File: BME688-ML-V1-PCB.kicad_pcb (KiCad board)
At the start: 2 copper layers, 25.4 x 25.4 mm, 33 parts, among them SW1 434133025816, U1 STM32L431KBU6TR, U2 BME688, U3 BME688

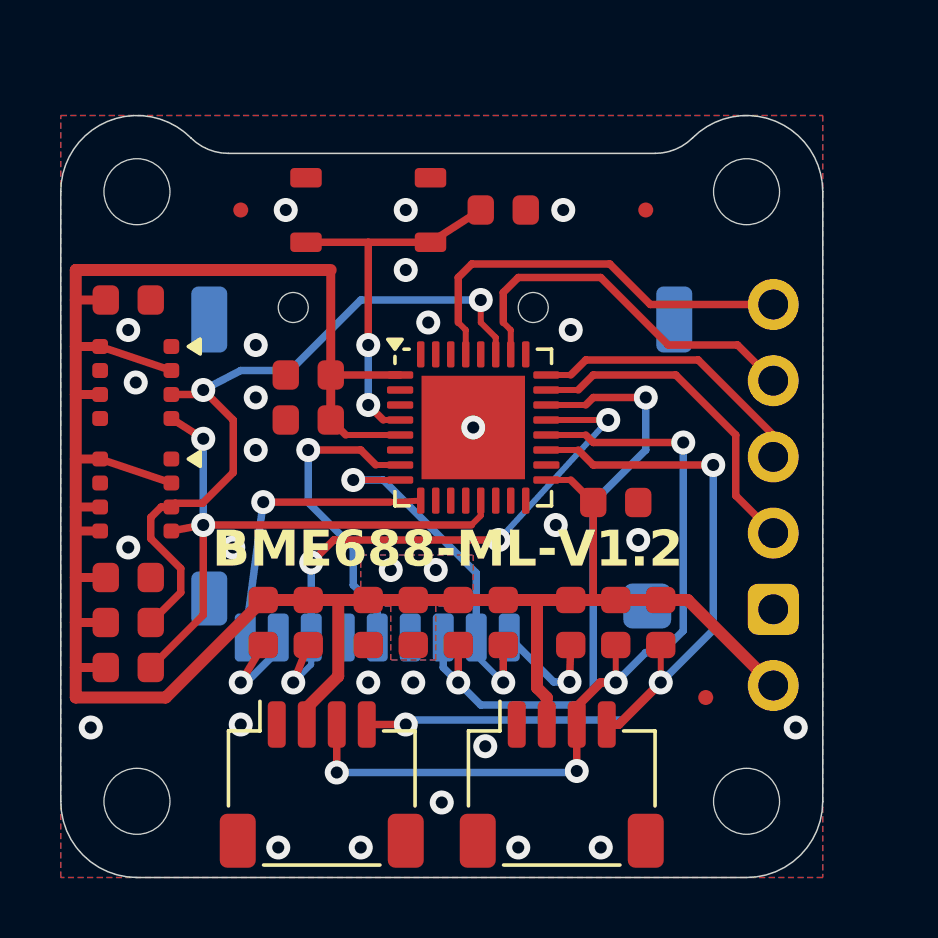
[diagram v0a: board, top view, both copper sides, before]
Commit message: fillet tracks for more beauty
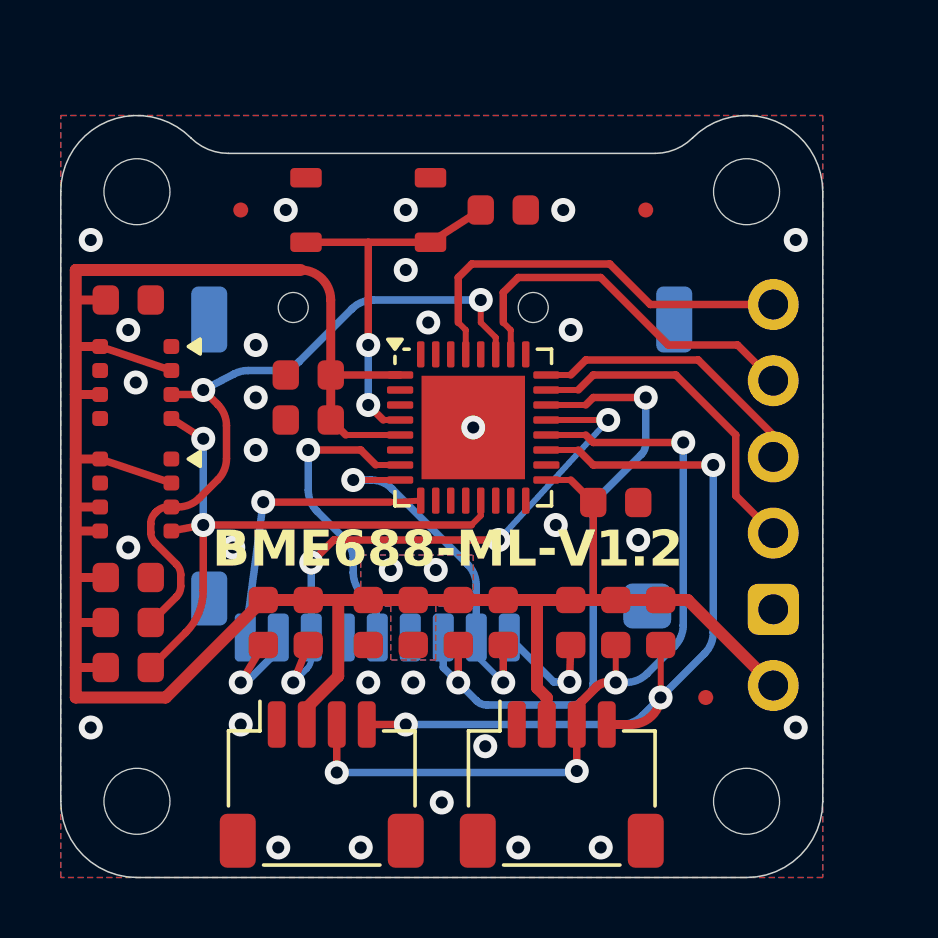
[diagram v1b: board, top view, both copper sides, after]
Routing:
- net I2C3-SDA: track 24.4 -> 23.7 mm
- net I2C1-SCL: track 27.8 -> 28.3 mm
- net GND: vias 27 -> 29

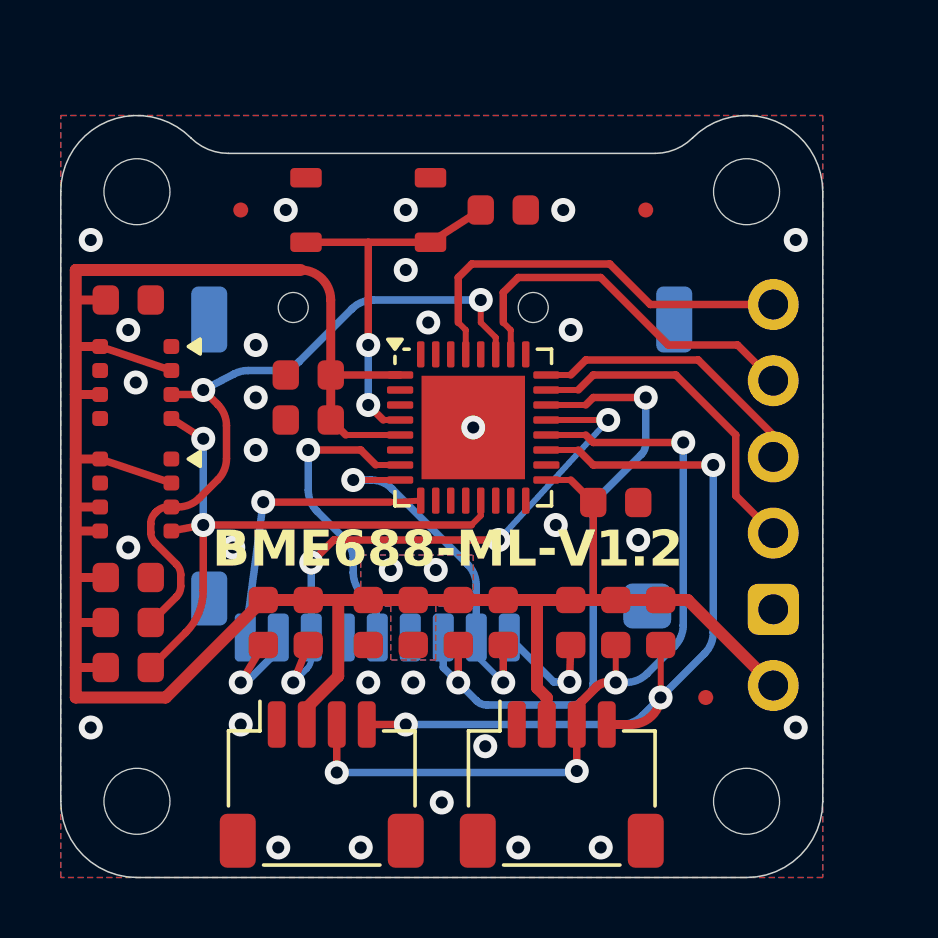
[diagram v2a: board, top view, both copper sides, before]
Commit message: Add #3 and fix #5
Add application button
Add RGB led
Move SD-card connector to align inserted card with PCB edge
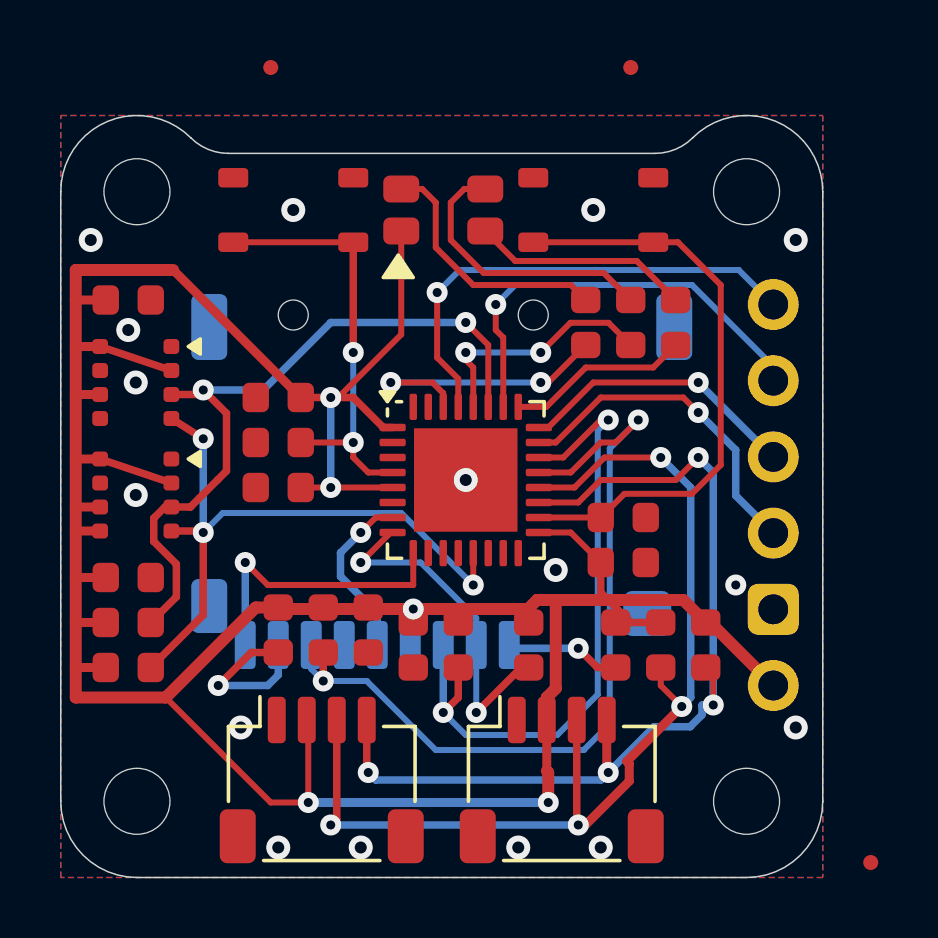
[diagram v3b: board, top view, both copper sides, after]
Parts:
- added C9: KGM15AR71C104KT, 1projectLibrary:C_0603_nominal, F.Cu at (133.1, 76.9)
- added D1: LED_RGBA_150141M173100, 1projectLibrary:RGB_LED_150141M173100, F.Cu at (127.0, 66.7)
- added R10: CR0603-FX-4701ELF, 1projectLibrary:R_0603_nominal, F.Cu at (134.8, 70.4)
- added R11: CR0603-FX-4701ELF, 1projectLibrary:R_0603_nominal, F.Cu at (133.3, 70.4)
- added R12: CR0603-FX-4701ELF, 1projectLibrary:R_0603_nominal, F.Cu at (131.8, 70.4)
- added SW2: 434133025816, 1projectLibrary:Wurth-434133025816, F.Cu at (132.1, 66.7)
- moved C6 10.8 mm to (121.5, 74.4), turned to 180 degrees
- moved F1 7.78 mm to (141.3, 88.4)
- moved F2 4.85 mm to (121.3, 61.9)
- moved F3 4.78 mm to (133.3, 61.9)
- moved SW1 2.50 mm to (122.0, 66.7)
- moved C4 2.46 mm to (121.5, 75.9)
- moved C7 2.02 mm to (133.1, 78.4)
- moved U1 1.77 mm to (127.8, 75.7)
- moved R4 1.68 mm to (132.8, 81.2)
- moved R6 1.68 mm to (135.8, 81.2)
- moved R7 1.68 mm to (134.3, 81.2)
- moved C1 1.25 mm to (121.5, 72.9)
- moved R3 1.13 mm to (129.9, 81.2)
- moved C2 0.75 mm to (126.0, 81.2)
- moved R1 0.75 mm to (127.5, 81.2)
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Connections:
- U1 pad 18: GND -> Net-(U1-PA8)
- U1 pad 25: GND -> Net-(U1-PA15)
- U1 pad 28: GND -> Net-(U1-PB5)
- U1 pad 30: GND -> Net-(U1-UART1_RX)
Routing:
- net +3.3V: track 85.0 -> 110.2 mm, vias 2 -> 5
- net Net-(U1-PA8): track 0.00 -> 19.6 mm
- net Net-(D1-GK): track 0.00 -> 9.41 mm
- net Net-(U1-UART1_RX): track 0.00 -> 9.37 mm, vias 0 -> 2
- net Net-(D1-BK): track 0.00 -> 8.56 mm
- net SPI-MISO: track 19.6 -> 27.7 mm, vias 4 -> 2
- net Net-(U1-PB5): track 0.00 -> 8.13 mm, vias 0 -> 2
- net I2C1-SDA: track 28.5 -> 36.4 mm
- net Net-(D1-RK): track 0.00 -> 7.66 mm
- net Net-(U1-PA15): track 0.00 -> 6.10 mm
- net SPI1-CLK: track 10.3 -> 5.81 mm
- net I2C1-SCL: track 28.3 -> 32.1 mm, vias 3 -> 4
- net UART1-TX: track 14.0 -> 16.1 mm, vias 0 -> 1
- net Net-(CONN3-NC8): track 3.58 -> 5.60 mm
- net SWO: track 12.8 -> 14.6 mm, vias 0 -> 1
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- removed copper zone on B.Cu, net +3.3V
- removed copper zone on F.Cu, net +3.3V
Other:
- board text removed: "BME688-ML-V1.2"

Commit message: Fix overlapping courtyard
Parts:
- moved F1 21.7 mm to (122.3, 77.9)
- moved F3 15.9 mm to (135.8, 77.7)
- moved F2 7.57 mm to (120.3, 69.4)
- moved SW2 0.08 mm to (132.0, 66.7)
